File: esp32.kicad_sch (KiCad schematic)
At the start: 23 parts, among them J7 serial, Q2 Q_NPN_BCE, Q3 Q_NPN_BCE, U26 ESP32-WROOM-32D, U28 LMZM23601

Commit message: update partnumbers to what was bought
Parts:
- U28: PN LMZM23601 -> LMZM23601V3SILR
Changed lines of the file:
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@@
 			)
 		)
-		(property "PN" "LMZM23601"
+		(property "PN" "LMZM23601V3SILR "
 			(at 63.5 33.02 0)
 			(effects

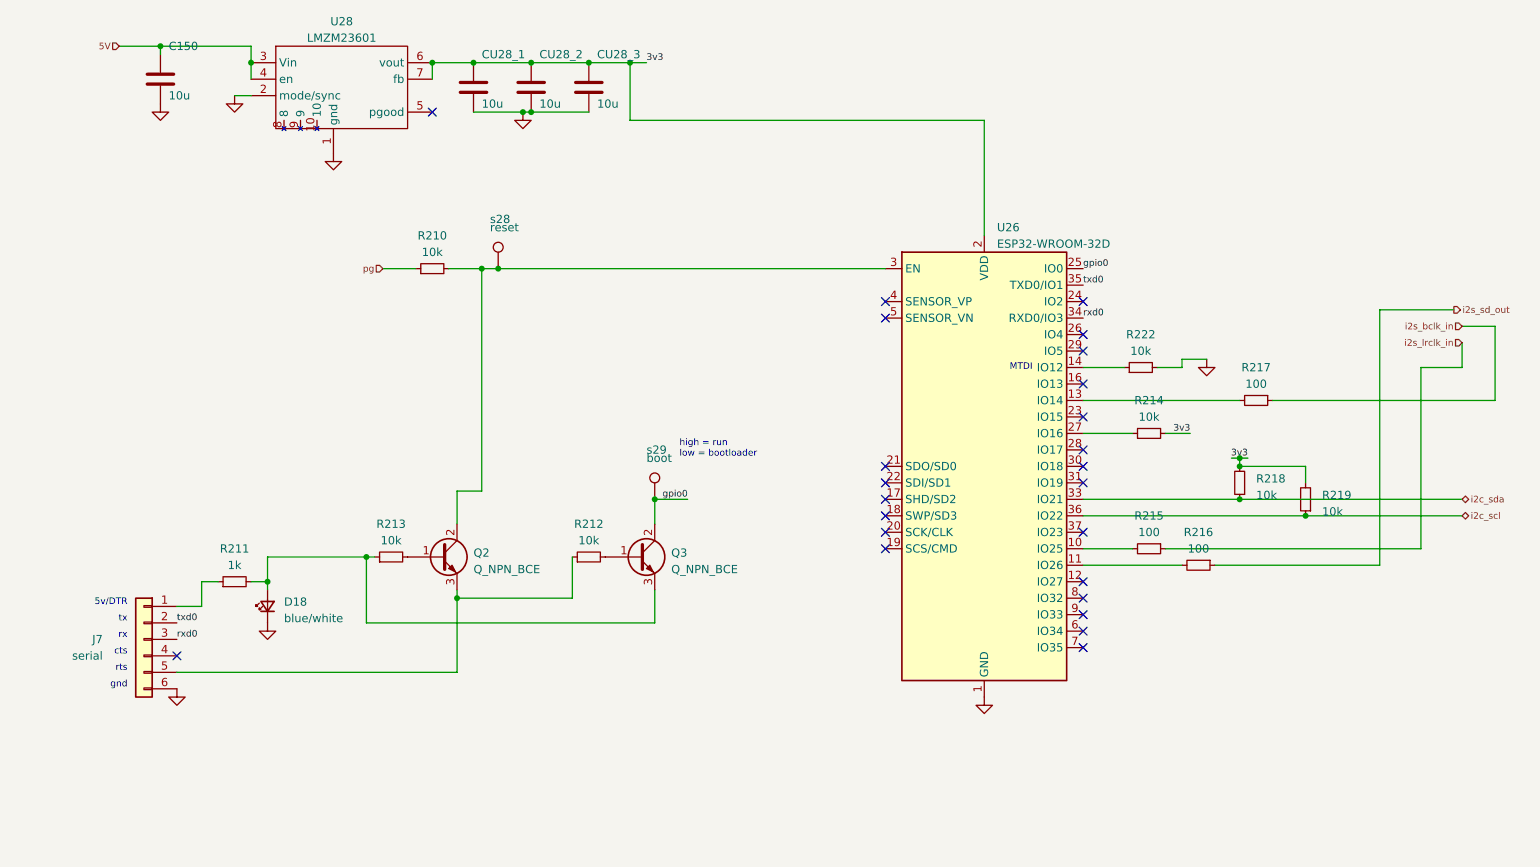
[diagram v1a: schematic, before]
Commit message: work on bugs
* align parts
* enlarge cercaps
* fix ak caps
* improve jack footprint
* fix lmr stencil openings
* remove one ldo
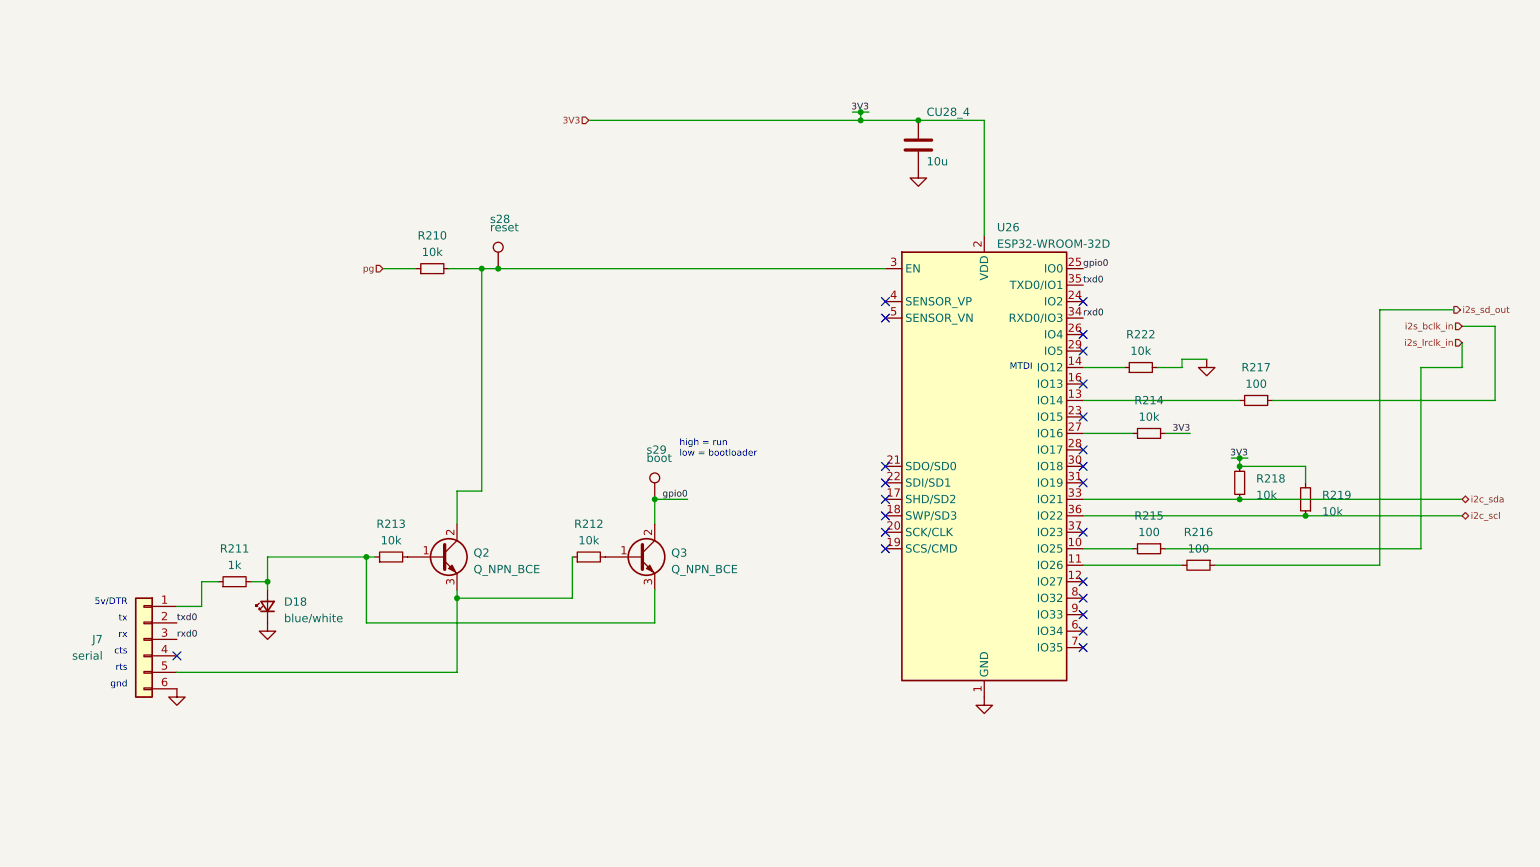
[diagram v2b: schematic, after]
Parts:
- removed C150, CU28_1, CU28_2, CU28_3: 10u, invendelirium_audio:C_0603, symbol Device:C
- removed U28: LMZM23601, invendelirium_general:LMZM23601, symbol invendelirium_ic:LMZM23601
- added CU28_4: 10u, invendelirium_audio:C_0603_larger, symbol Device:C
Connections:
- net GND: now also CU28_4.2
- net 3v3 renamed 3V3
- net 3V3: now also CU28_4.1
- no-connect marks 24 -> 23

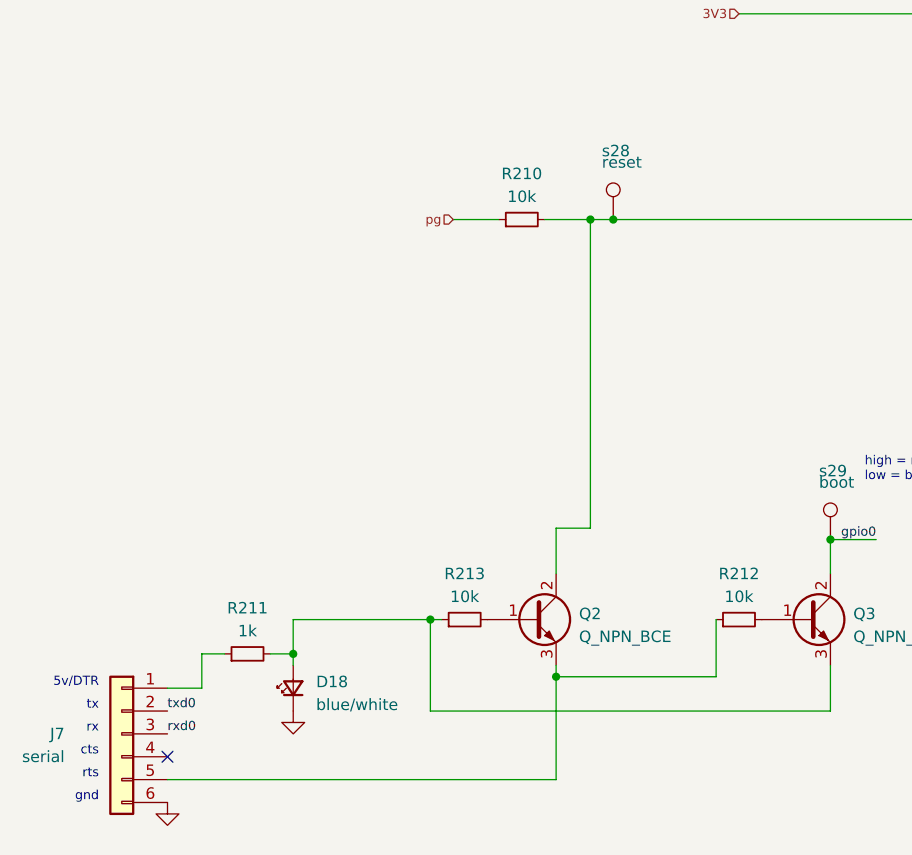
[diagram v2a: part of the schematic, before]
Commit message: add cap for esp autoreset
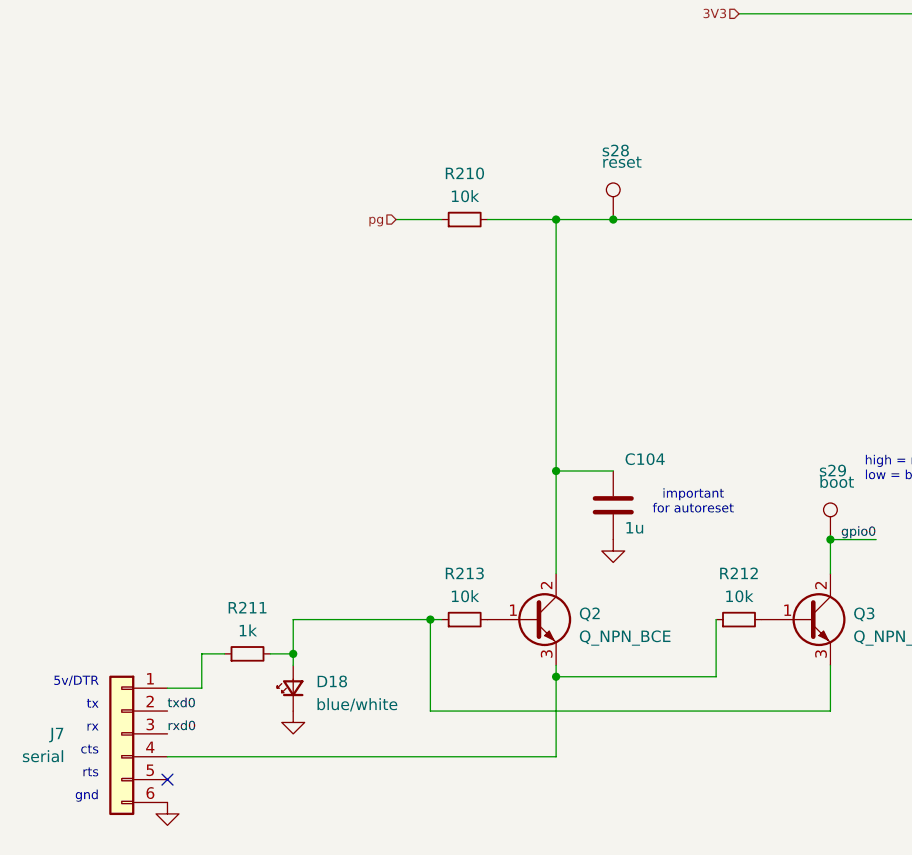
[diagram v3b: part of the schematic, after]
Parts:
- added C104: 1u, invendelirium_audio:C_0603_larger, symbol Device:C
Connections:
- net GND: now also C104.2
- net at Q2.2 (C), R210.2, U26.3 (EN)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: now also C104.1
- net at Q2.3 (E), R212.1: now also J7.4 (Pin_4); no longer J7.5 (Pin_5)
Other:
- note added: "important for autoreset"
- moved on the sheet: R210
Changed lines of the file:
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@@
 	(paper "A4")
-	(junction
-		(at 83.82 59.69)
-		(diameter 0)
-		(color 0 0 0 0)
-	)
 	(junction
 		(at 200.66 88.9)
@@
 	)
 	(junction
+		(at 80.01 59.69)
+		(diameter 0)
+		(color 0 0 0 0)
+	)
+	(junction
 		(at 151.13 36.83)
 		(diameter 0)
@@
 	)
 	(junction
+		(at 80.01 87.63)
+		(diameter 0)
+		(color 0 0 0 0)
+	)
+	(junction
 		(at 200.66 95.25)
 		(diameter 0)
@@
 	)
 	(no_connect
-		(at 36.83 119.38)
+		(at 36.83 121.92)
 	)
 	(no_connect
@@
 	(wire
 		(pts
-			(xy 80.01 110.49) (xy 80.01 121.92)
+			(xy 80.01 59.69) (xy 86.36 59.69)
+		)
+		(stroke
+			(width 0)
+			(type default)
+		)
+	)
+	(wire
+		(pts
+			(xy 80.01 110.49) (xy 80.01 119.38)
 		)
 		(stroke
@@
 	(wire
 		(pts
+			(xy 80.01 87.63) (xy 86.36 87.63)
+		)
+		(stroke
+			(width 0)
+			(type default)
+		)
+	)
+	(wire
+		(pts
 			(xy 234.95 74.93) (xy 228.6 74.93)
 		)
@@
 	(wire
 		(pts
-			(xy 78.74 59.69) (xy 83.82 59.69)
-		)
-		(stroke
-			(width 0)
-			(type default)
-		)
-	)
-	(wire
-		(pts
-			(xy 80.01 121.92) (xy 36.83 121.92)
+			(xy 72.39 59.69) (xy 80.01 59.69)
+		)
+		(stroke
+			(width 0)
+			(type default)
+		)
+	)
+	(wire
+		(pts
+			(xy 80.01 119.38) (xy 36.83 119.38)
 		)
 		(stroke
@@
 	(wire
 		(pts
+			(xy 80.01 87.63) (xy 80.01 99.06)
+		)
+		(stroke
+			(width 0)
+			(type default)
+		)
+	)
+	(wire
+		(pts
 			(xy 50.8 104.14) (xy 66.04 104.14)
 		)
@@
 	(wire
 		(pts
-			(xy 80.01 93.98) (xy 83.82 93.98)
-		)
-		(stroke
-			(width 0)
-			(type default)
-		)
-	)
-	(wire
-		(pts
-			(xy 80.01 99.06) (xy 80.01 93.98)
-		)
-		(stroke
-			(width 0)
-			(type default)
-		)
-	)
-	(wire
-		(pts
 			(xy 110.49 114.3) (xy 110.49 109.22)
 		)
@@
 	(wire
 		(pts
-			(xy 68.58 59.69) (xy 73.66 59.69)
+			(xy 62.23 59.69) (xy 67.31 59.69)
 		)
 		(stroke
@@
 	(wire
 		(pts
-			(xy 83.82 59.69) (xy 83.82 93.98)
+			(xy 80.01 59.69) (xy 80.01 87.63)
 		)
 		(stroke
@@
 		(pts
 			(xy 176.53 74.93) (xy 182.88 74.93)
-		)
-		(stroke
-			(width 0)
-			(type default)
-		)
-	)
-	(wire
-		(pts
-			(xy 83.82 59.69) (xy 86.36 59.69)
 		)
 		(stroke
@@
 		)
 	)
+	(text "important\nfor autoreset"
+		(exclude_from_sim no)
+		(at 95.25 91.186 0)
+		(effects
+			(font
+				(size 1.016 1.016)
+			)
+		)
+	)
 	(text "rx"
 		(exclude_from_sim no)
@@
 	(hierarchical_label "pg"
 		(shape input)
-		(at 68.58 59.69 180)
+		(at 62.23 59.69 180)
 		(fields_autoplaced yes)
 		(effects
@@
 	)
 	(symbol
+		(lib_id "Device:C")
+		(at 86.36 91.44 0)
+		(unit 1)
+		(exclude_from_sim no)
+		(in_bom yes)
+		(on_board yes)
+		(dnp no)
+		(property "Reference" "C104"
+			(at 87.63 86.36 0)
+			(effects
+				(font
+					(size 1.27 1.27)
+				)
+				(justify left)
+			)
+		)
+		(property "Value" "1u"
+			(at 87.63 93.98 0)
+			(effects
+				(font
+					(size 1.27 1.27)
+				)
+				(justify left)
+			)
+		)
+		(property "Footprint" "invendelirium_audio:C_0603_larger"
+			(at 87.3252 95.25 0)
+			(effects
+				(font
+					(size 1.27 1.27)
+				)
+				(hide yes)
+			)
+		)
+		(property "Datasheet" "~"
+			(at 86.36 91.44 0)
+			(effects
+				(font
+					(size 1.27 1.27)
+				)
+				(hide yes)
+			)
+		)
+		(property "Description" ""
+			(at 86.36 91.44 0)
+			(effects
+				(font
+					(size 1.27 1.27)
+				)
+				(hide yes)
+			)
+		)
+		(property "Voltage" "16V"
+			(at 86.36 91.44 0)
+			(effects
+				(font
+					(size 1.27 1.27)
+				)
+				(hide yes)
+			)
+		)
+		(property "Sim.Device" ""
+			(at 86.36 91.44 0)
+			(effects
+				(font
+					(size 1.27 1.27)
+				)
+				(hide yes)
+			)
+		)
+		(property "Sim.Library" ""
+			(at 86.36 91.44 0)
+			(effects
+				(font
+					(size 1.27 1.27)
+				)
+				(hide yes)
+			)
+		)
+		(property "Sim.Name" ""
+			(at 86.36 91.44 0)
+			(effects
+				(font
+					(size 1.27 1.27)
+				)
+				(hide yes)
+			)
+		)
+		(property "Sim.Pins" ""
+			(at 86.36 91.44 0)
+			(effects
+				(font
+					(size 1.27 1.27)
+				)
+				(hide yes)
+			)
+		)
+		(pin "1"
+		)
+		(pin "2"
+		)
+		(instances
+			(project "uberamp1"
+				(path "/310059c1-d84b-43e2-9c9a-0e426c534a12/c7f5e7f4-a933-42eb-8650-67011ef6e24d"
+					(reference "C104")
+					(unit 1)
+				)
+			)
+		)
+	)
+	(symbol
 		(lib_id "power:GND")
 		(at 161.29 125.73 0)
@@
 	)
 	(symbol
+		(lib_id "power:GND")
+		(at 86.36 95.25 0)
+		(unit 1)
+		(exclude_from_sim no)
+		(in_bom yes)
+		(on_board yes)
+		(dnp no)
+		(fields_autoplaced yes)
+		(property "Reference" "#PWR0209"
+			(at 86.36 101.6 0)
+			(effects
+				(font
+					(size 1.27 1.27)
+				)
+				(hide yes)
+			)
+		)
+		(property "Value" "GND"
+			(at 86.36 100.33 0)
+			(effects
+				(font
+					(size 1.27 1.27)
+				)
+				(hide yes)
+			)
+		)
+		(property "Footprint" ""
+			(at 86.36 95.25 0)
+			(effects
+				(font
+					(size 1.27 1.27)
+				)
+				(hide yes)
+			)
+		)
+		(property "Datasheet" ""
+			(at 86.36 95.25 0)
+			(effects
+				(font
+					(size 1.27 1.27)
+				)
+				(hide yes)
+			)
+		)
+		(property "Description" ""
+			(at 86.36 95.25 0)
+			(effects
+				(font
+					(size 1.27 1.27)
+				)
+				(hide yes)
+			)
+		)
+		(pin "1"
+		)
+		(instances
+			(project "uberamp1"
+				(path "/310059c1-d84b-43e2-9c9a-0e426c534a12/c7f5e7f4-a933-42eb-8650-67011ef6e24d"
+					(reference "#PWR0209")
+					(unit 1)
+				)
+			)
+		)
+	)
+	(symbol
 		(lib_id "Device:R_Small")
 		(at 210.82 95.25 180)
@@
 	(symbol
 		(lib_id "Device:R_Small")
-		(at 76.2 59.69 90)
+		(at 69.85 59.69 90)
 		(unit 1)
 		(exclude_from_sim no)
@@
 		(fields_autoplaced yes)
 		(property "Reference" "R210"
-			(at 76.2 54.61 90)
+			(at 69.85 54.61 90)
 			(effects
 				(font
@@
 		)
 		(property "Value" "10k"
-			(at 76.2 57.15 90)
+			(at 69.85 57.15 90)
 			(effects
 				(font
@@
 		)
 		(property "Footprint" "invendelirium_audio:R_0603"
-			(at 76.2 59.69 0)
+			(at 69.85 59.69 0)
 			(effects
 				(font
@@
 		)
 		(property "Datasheet" "~"
-			(at 76.2 59.69 0)
+			(at 69.85 59.69 0)
 			(effects
 				(font
@@
 		)
 		(property "Description" ""
-			(at 76.2 59.69 0)
+			(at 69.85 59.69 0)
 			(effects
 				(font
@@
 		)
 		(property "Sim.Device" ""
-			(at 76.2 59.69 0)
+			(at 69.85 59.69 0)
 			(effects
 				(font
@@
 		)
 		(property "Sim.Library" ""
-			(at 76.2 59.69 0)
+			(at 69.85 59.69 0)
 			(effects
 				(font
@@
 		)
 		(property "Sim.Name" ""
-			(at 76.2 59.69 0)
+			(at 69.85 59.69 0)
 			(effects
 				(font
@@
 		)
 		(property "Sim.Pins" ""
-			(at 76.2 59.69 0)
-			(effects
-				(font
+			(at 69.85 59.69 0)
+			(effects
+				(font

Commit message: work on bugs
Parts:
- removed R218, R219: 10k, invendelirium_audio:R_0603, symbol Device:R_Small
- added J11: Conn_01x04, Connector_JST:JST_GH_BM04B-GHS-TBT_1x04-1MP_P1.25mm_Vertical, symbol Connector_Generic:Conn_01x04
- added LED5: blink, invendelirium_general:D_0805, symbol Device:LED
- added LED6: blink2, invendelirium_general:D_0805, symbol Device:LED
- added R243, R244: 100, invendelirium_audio:R_0603, symbol Device:R_Small
- added R245, R246: 2.7K, invendelirium_audio:R_0603, symbol Device:R_Small
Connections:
- net GND: now also J11.4 (Pin_4), LED5.1 (K), LED6.1 (K)
- net i2c_scl: now also J11.2 (Pin_2)
- net i2c_sda: now also J11.3 (Pin_3)
- net rxd0: now also R243.1; no longer J7.3 (Pin_3)
- net txd0: now also R244.1; no longer J7.2 (Pin_2)
- net io27: now reaches U26.12 (IO27)
- net io27: now also R246.2
- net io13: now reaches U26.16 (IO13)
- net io13: now also R245.2
- new net: LED5.2 (A), R245.1
- new net: LED6.2 (A), R246.1
- new net: J7.2 (Pin_2), R244.2
- new net: J7.3 (Pin_3), R243.2
- no-connect marks 23 -> 20
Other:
- note added: "vcc scl sda gnd"
- moved on the sheet: J7
